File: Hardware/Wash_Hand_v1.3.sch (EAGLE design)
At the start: 46 parts, among them IC1 LM358D, J1 I2C, J2 ICSP, J3 SPI, J5 EXT_VCC, J6 6_PIN_SERIAL_CABLEPTH, Q1 16.0 Mhz, U1 328P, U2 5V

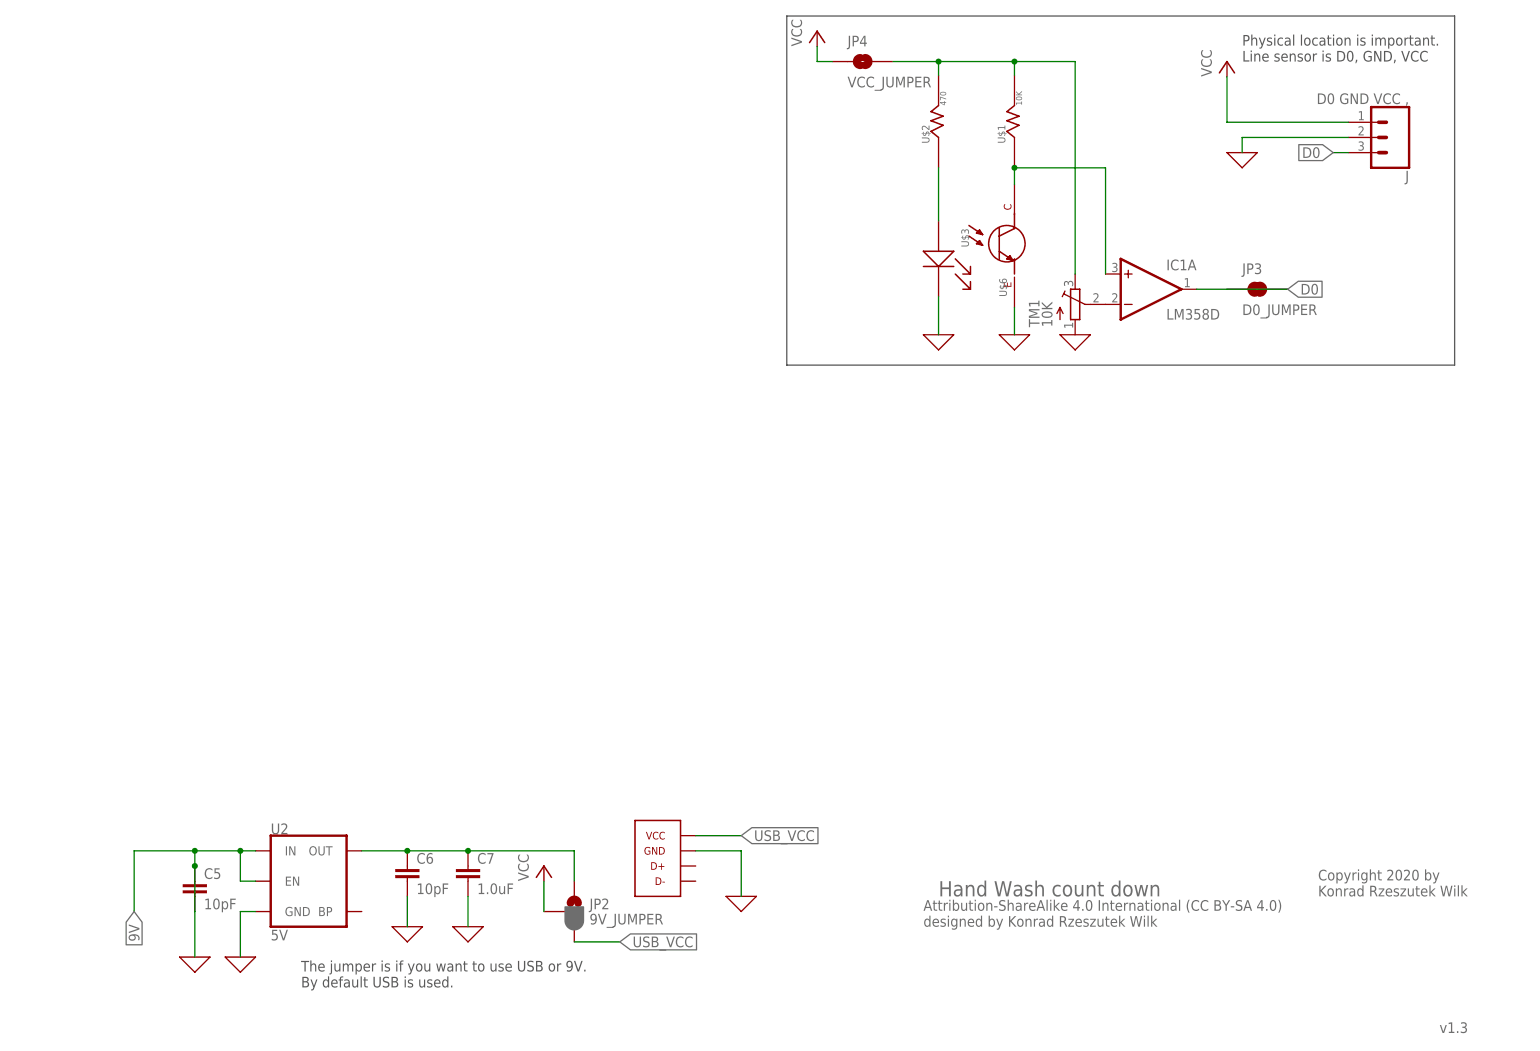
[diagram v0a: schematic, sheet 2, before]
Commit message: Board/Schematic: Add test-points and adjust SMT to be aligned.
Added TEST-POINT3X4 for:
 - TP1, 5V VCC
 - TP2, 5V USB VCC
 - TP3, IR Detector VCC
 - TP4, IR Emitter VCC
 - TP5, 9V VCC

Signed-off-by: Konrad Rzeszutek Wilk <konrad@kernel.org>
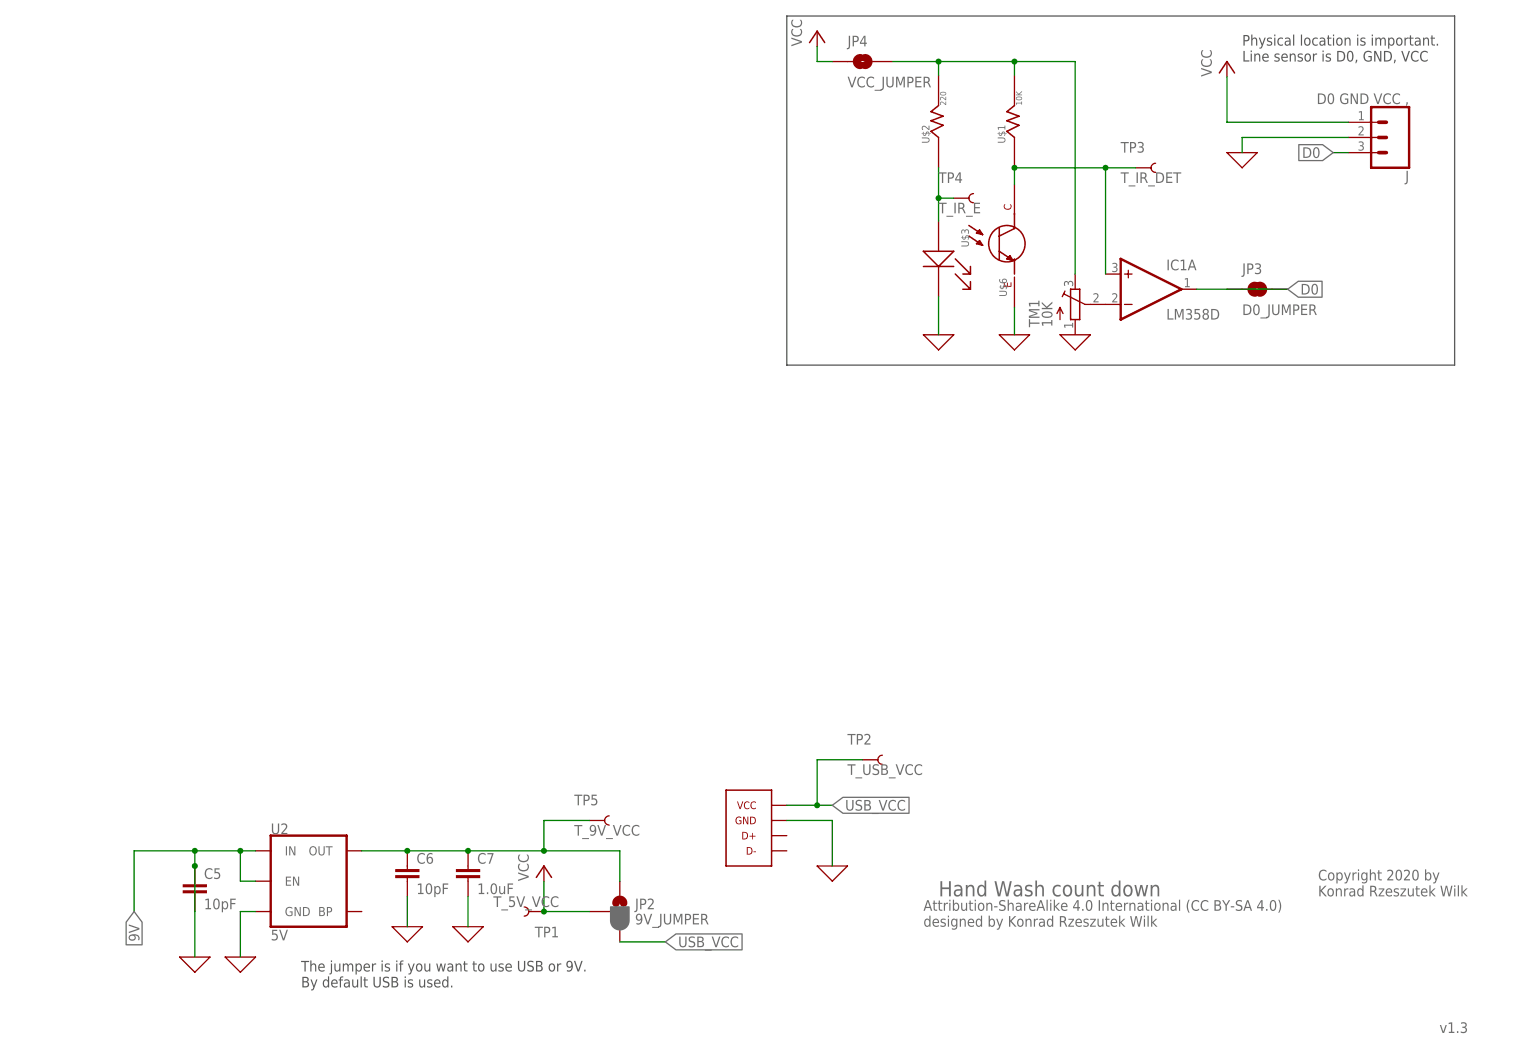
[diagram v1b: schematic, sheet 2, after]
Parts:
- added TP1: T_5V_VCC, SparkFun-Connectors:TEST-POINT3X4
- added TP2: T_USB_VCC, SparkFun-Connectors:TEST-POINT3X4
- added TP3: T_IR_DET, SparkFun-Connectors:TEST-POINT3X4
- added TP4: T_IR_E, SparkFun-Connectors:TEST-POINT3X4
- added TP5: T_9V_VCC, SparkFun-Connectors:TEST-POINT3X4
- U$2: value 470 -> 220
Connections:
- net N$10: now also TP5.1
- net N$11: now also TP4.1
- net N$14: now also TP3.1
- net USB_VCC: now also TP2.1
- net VCC: now also TP1.1
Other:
- moved on the sheet: JP2

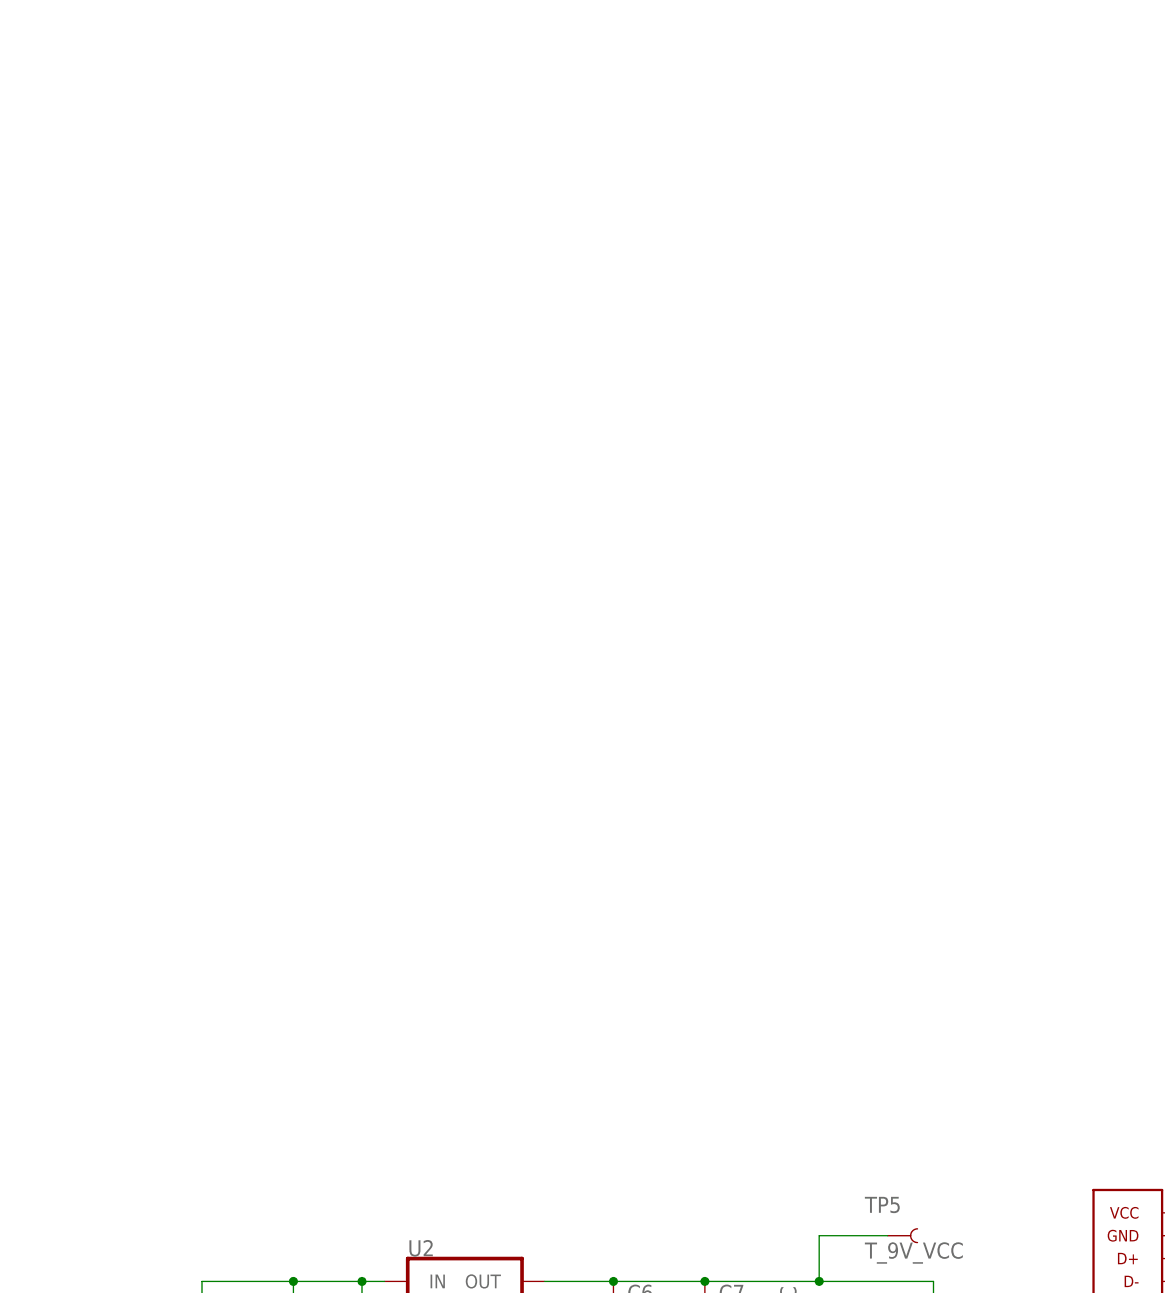
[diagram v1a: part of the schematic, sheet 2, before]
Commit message: Board/Schematic: Add MicroSD card for reading data for display
And that finishes v1.3 design.

 - Reworked connectors for programming via FTDI USB,
 - Built in line sensor,
 - Built in SD card for various texts,
 - SMD resistors and capacitors,
 - Test points,
 - 9V or 5V USB power option.

Now off to debug design, BOM, then routing.

Signed-off-by: Konrad Rzeszutek Wilk <konrad@kernel.org>
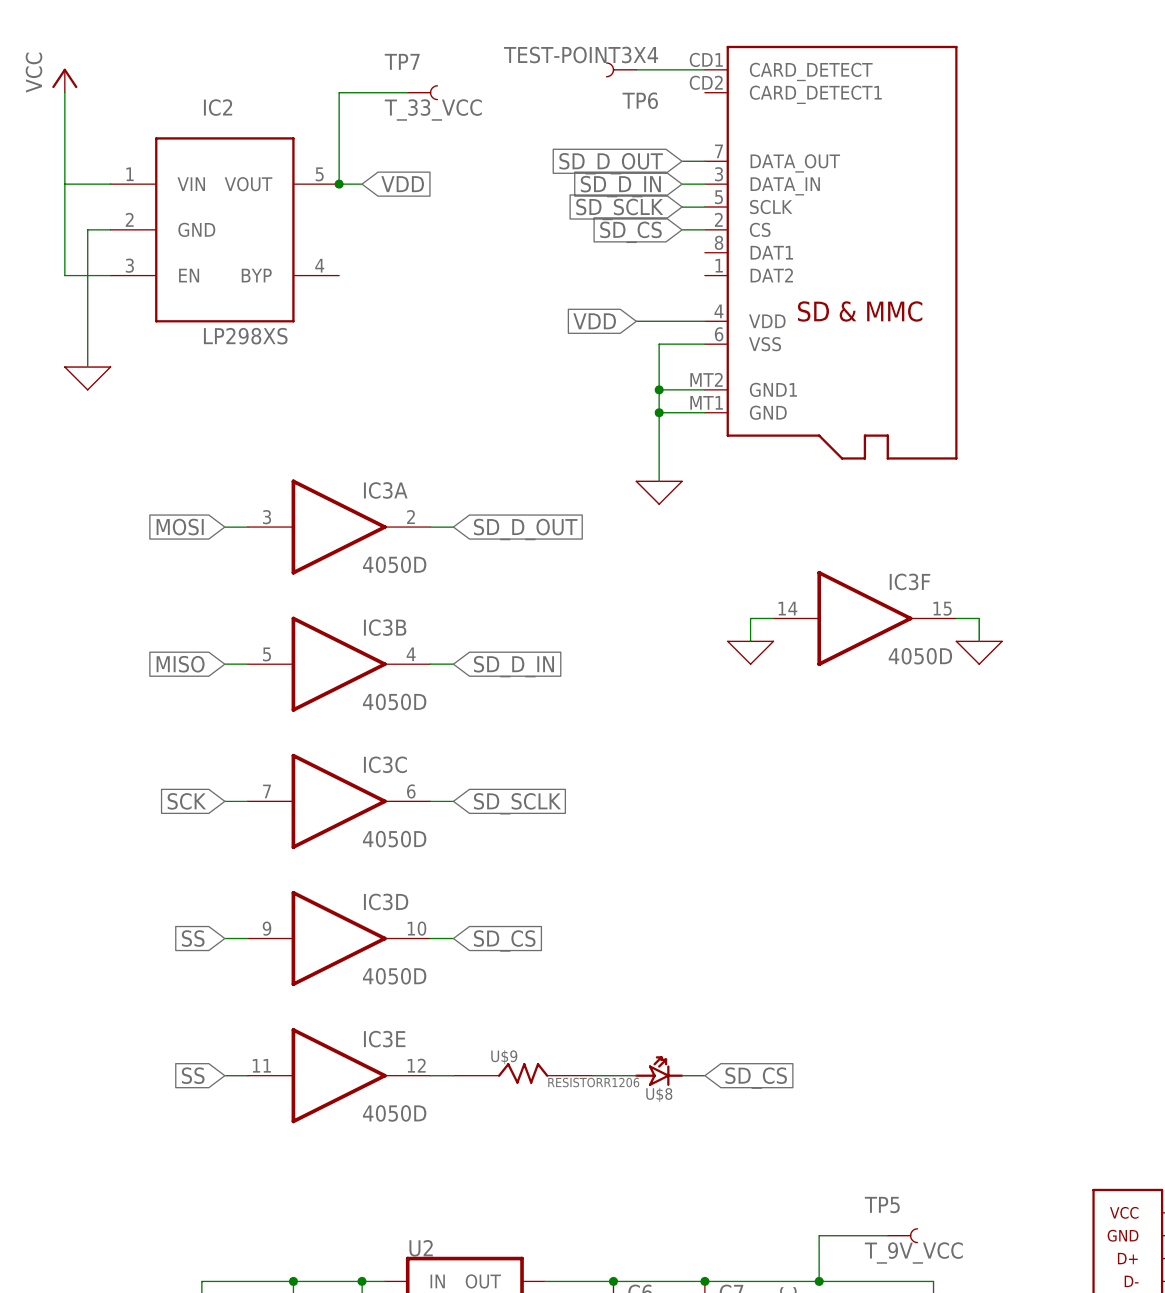
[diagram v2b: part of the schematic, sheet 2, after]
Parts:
- added IC2: LP298XS, adafruit:LP298XS
- added IC3: 4050D, 40xx:4050D
- added TP6: TEST-POINT3X4, SparkFun-Connectors:TEST-POINT3X4
- added TP7: T_33_VCC, SparkFun-Connectors:TEST-POINT3X4
- added U$7: MICROSD, adafruit:MICROSD
- added U$8: 5MM_LED, darnok_led:5MM_LED
- added U$9: RESISTORR1206, darnok_common:RESISTORR1206
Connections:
- new net N$17: TP6.1, U$7.CARD_DETECT
- new net N$21: IC3E.O, U$9.R_1
- new net N$22: U$8.PAD_$1, U$9.R_2
- new net SD_CS: IC3D.O, U$7.CS, U$8.PAD_$2
- new net SD_D_IN: IC3B.O, U$7.DATA_IN
- new net SD_D_OUT: IC3A.O, U$7.DATA_OUT
- new net SD_SCLK: IC3C.O, U$7.SCLK
- new net VDD: IC2.VOUT, TP7.1, U$7.VDD
- net 0: now also IC2.GND, IC3F.I, IC3F.O, U$7.GND, U$7.GND1, U$7.VSS
- net MISO: now also IC3B.I
- net MOSI: now also IC3A.I
- net SCK: now also IC3C.I
- net SS: now also IC3D.I, IC3E.I
- net VCC: now also IC2.EN, IC2.VIN

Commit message: Board/Schematic: s/VCC/VCC label/
As that makes it easier to switch in/out componets.

Signed-off-by: Konrad Rzeszutek Wilk <konrad@kernel.org>
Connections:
- removed net N$13: J6.4
- net VCC: now also J6.4
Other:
- moved on the sheet: C5, C6, C7, J3, JP2, TP1, TP2, TP5, U2

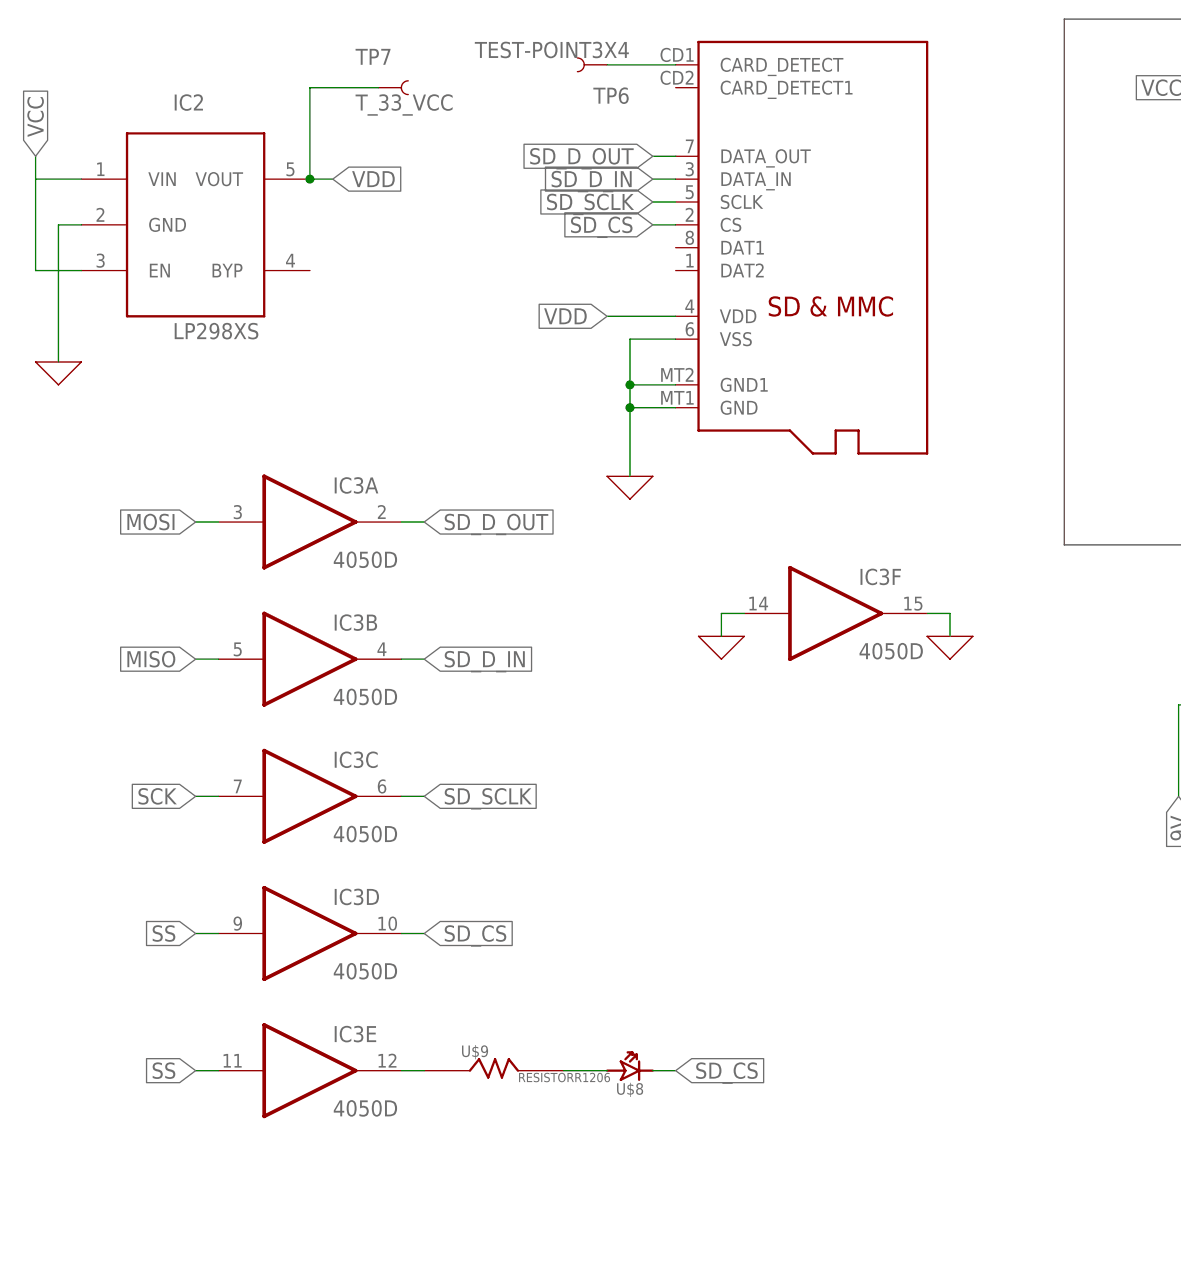
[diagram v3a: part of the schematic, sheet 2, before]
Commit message: Schematic: Fix 4050 not having VCC or GND, add 0.1uF and 2.2uF to LM358
Signed-off-by: Konrad Rzeszutek Wilk <konrad@kernel.org>
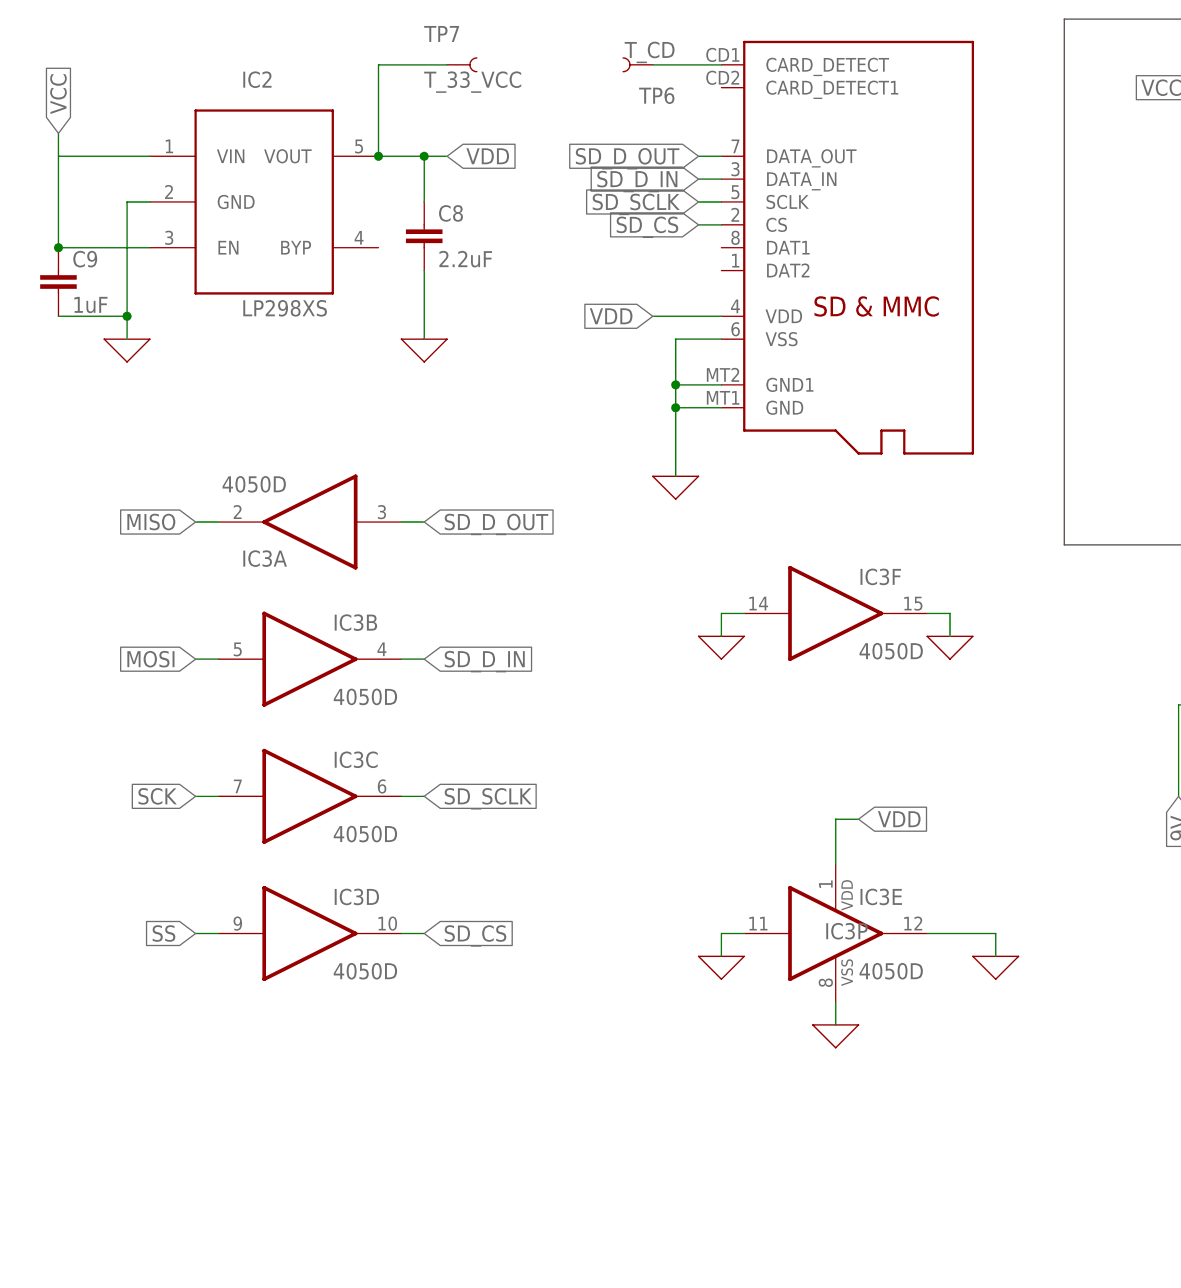
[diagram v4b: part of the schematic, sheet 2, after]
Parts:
- removed U$8: 5MM_LED, darnok_led:5MM_LED
- removed U$9: RESISTORR1206, darnok_common:RESISTORR1206
- added C8: 2.2uF, SparkFun-Capacitors:1.0UF-1206-50V-10%
- added C9: 1uF, SparkFun-Capacitors:1.0UF-1206-50V-10%
- TP6: value TEST-POINT3X4 -> T_CD
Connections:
- removed net N$21: IC3E.O, U$9.R_1
- removed net N$22: U$8.PAD_$1, U$9.R_2
- net 0: now also C8.2, C9.2, IC3E.I, IC3E.O, IC3P.VSS
- net MISO: now also IC3A.O; no longer IC3B.I
- net MOSI: now also IC3B.I; no longer IC3A.I
- net SD_CS: no longer U$8.PAD_$2
- net SD_D_OUT: now also IC3A.I; no longer IC3A.O
- net SS: no longer IC3E.I
- net VCC: now also C9.1
- net VDD: now also C8.1, IC3P.VDD
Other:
- moved on the sheet: IC2, IC3A, IC3E, TP6, TP7
